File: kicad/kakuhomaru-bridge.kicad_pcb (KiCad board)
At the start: 2 copper layers, 41.6 x 22.7 mm, 10 parts, among them J1 Conn_01x01, J10 Conn_01x01, J2 Conn_01x01, J3 Conn_01x01, J4 Conn_01x01, J5 Conn_01x01, J6 Conn_01x01, J7 Conn_01x01, J8 Conn_01x01, J9 Conn_01x01

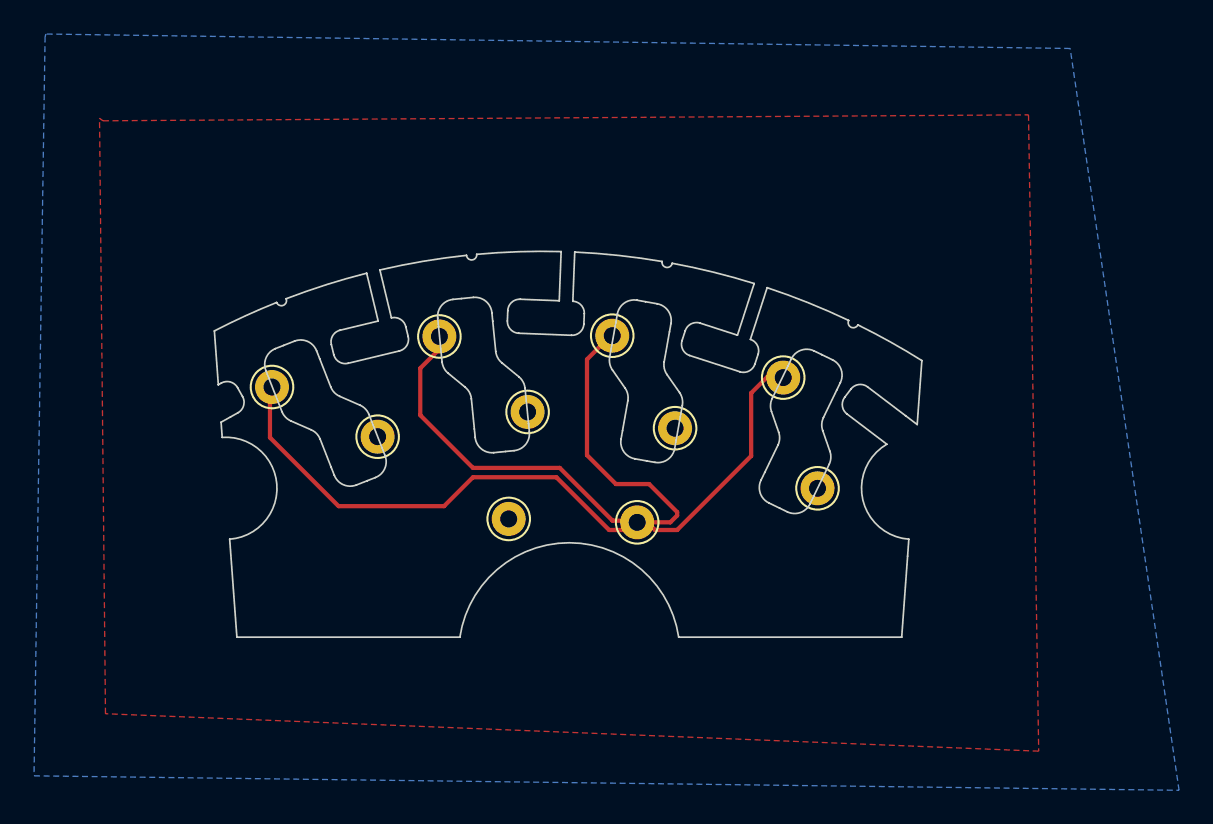
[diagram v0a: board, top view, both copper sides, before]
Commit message: Update PCB & case design
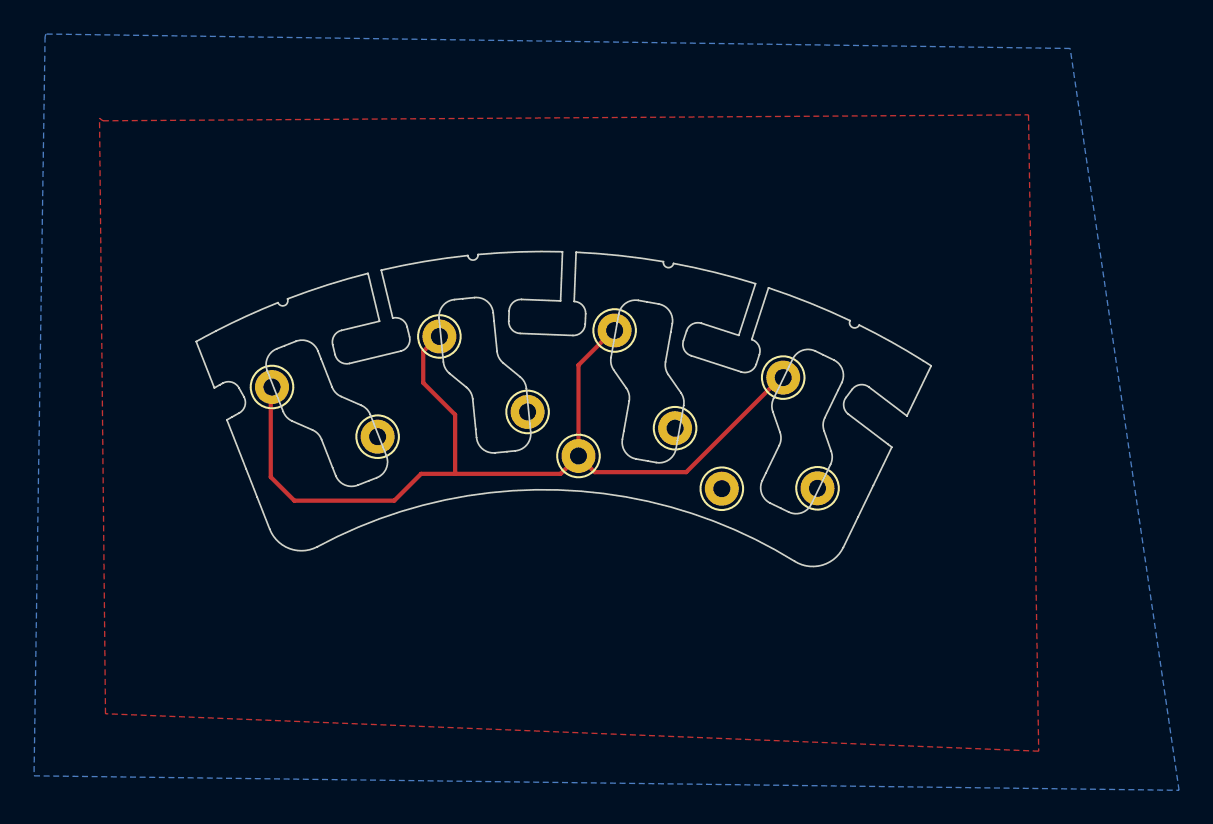
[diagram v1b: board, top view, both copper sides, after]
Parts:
- moved J8 12.7 mm to (115.3, 68.2)
- moved J5 5.21 mm to (106.9, 66.2)
- moved J6 0.34 mm to (109.0, 58.9)
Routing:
- net Net-(J1-Pin_1): track 81.9 -> 57.1 mm
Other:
- board size 41.6 x 22.7 mm -> 43.2 x 18.5 mm
